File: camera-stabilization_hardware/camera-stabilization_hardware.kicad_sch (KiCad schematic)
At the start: 17 parts, among them J1 Conn_01x05_Pin, J2 Conn_01x05_Pin, J3 AVR-ISP-6, U1 ULN2003, U2 ULN2003, U3 ATmega328PB-A, Y1 Crystal_GND24

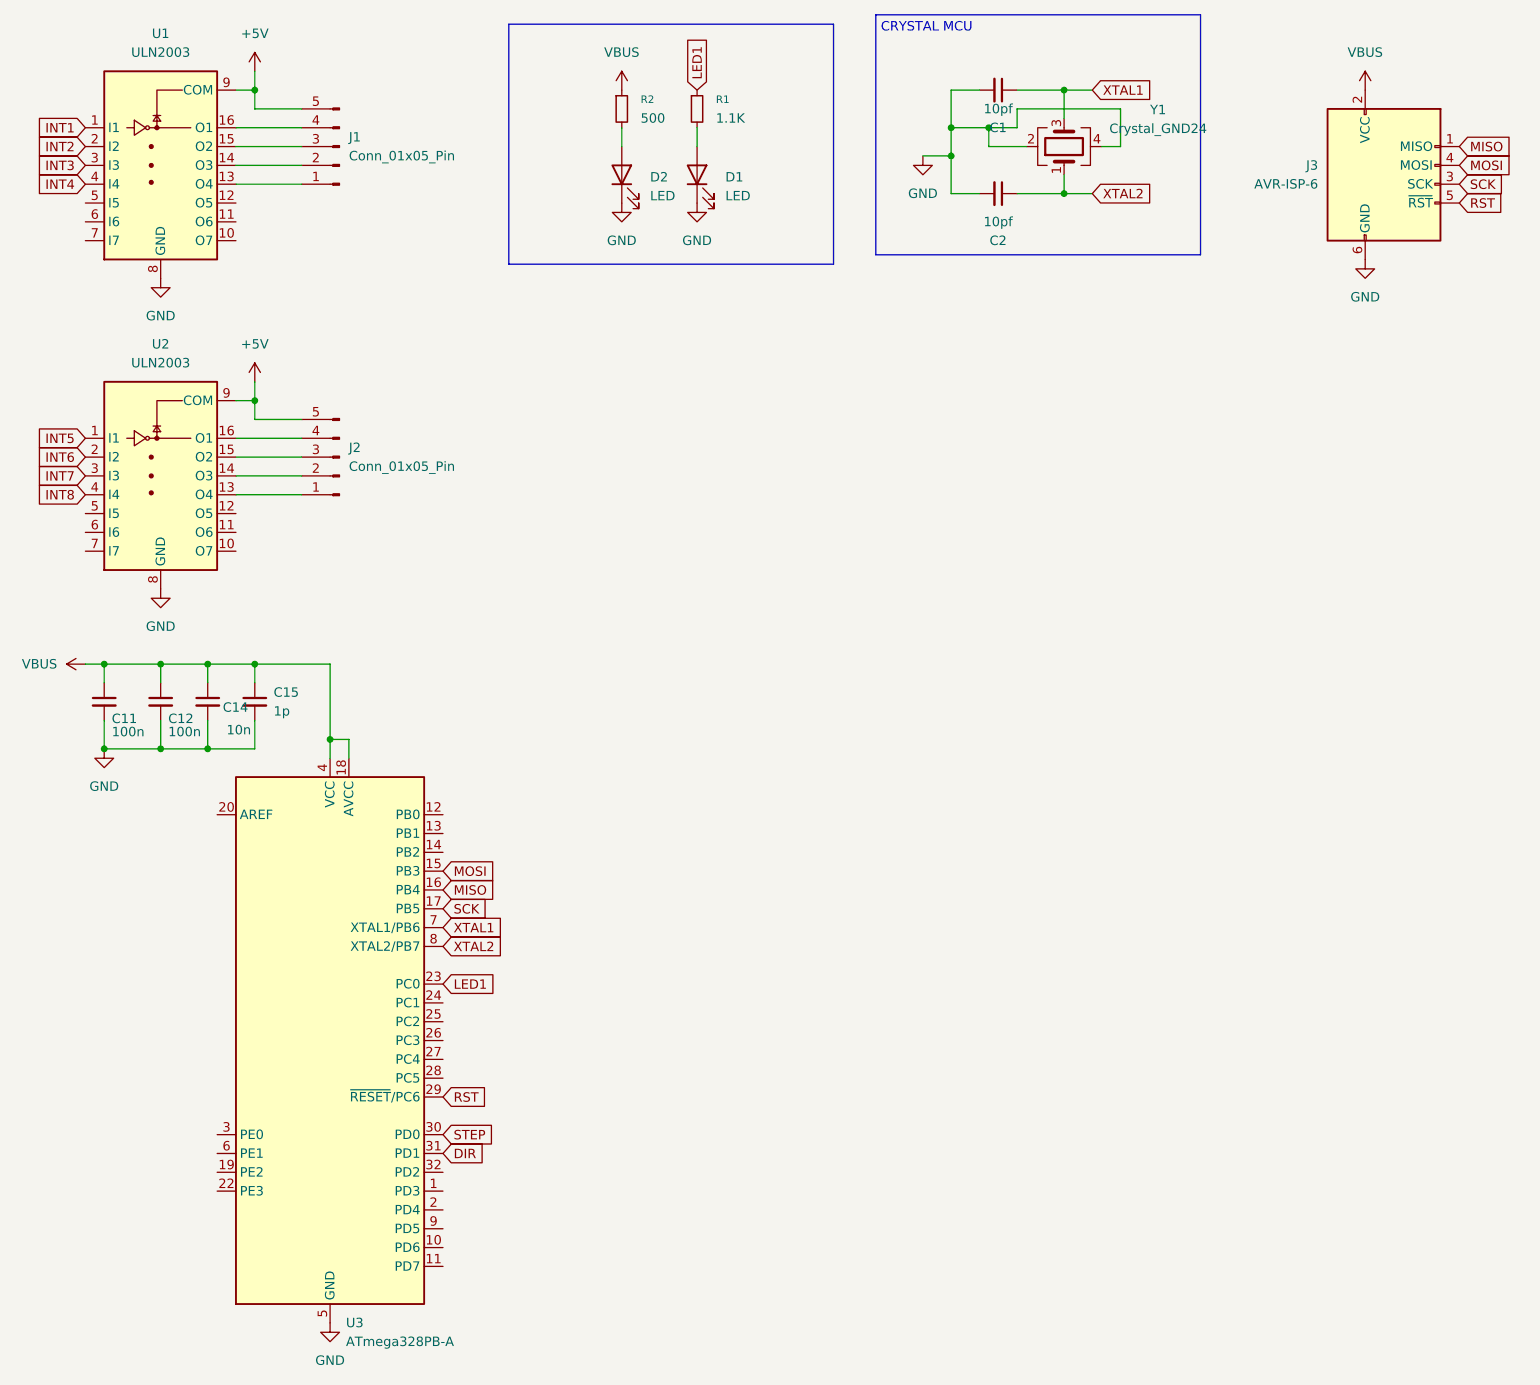
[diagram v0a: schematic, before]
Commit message: added pcb wiring camera stabilization
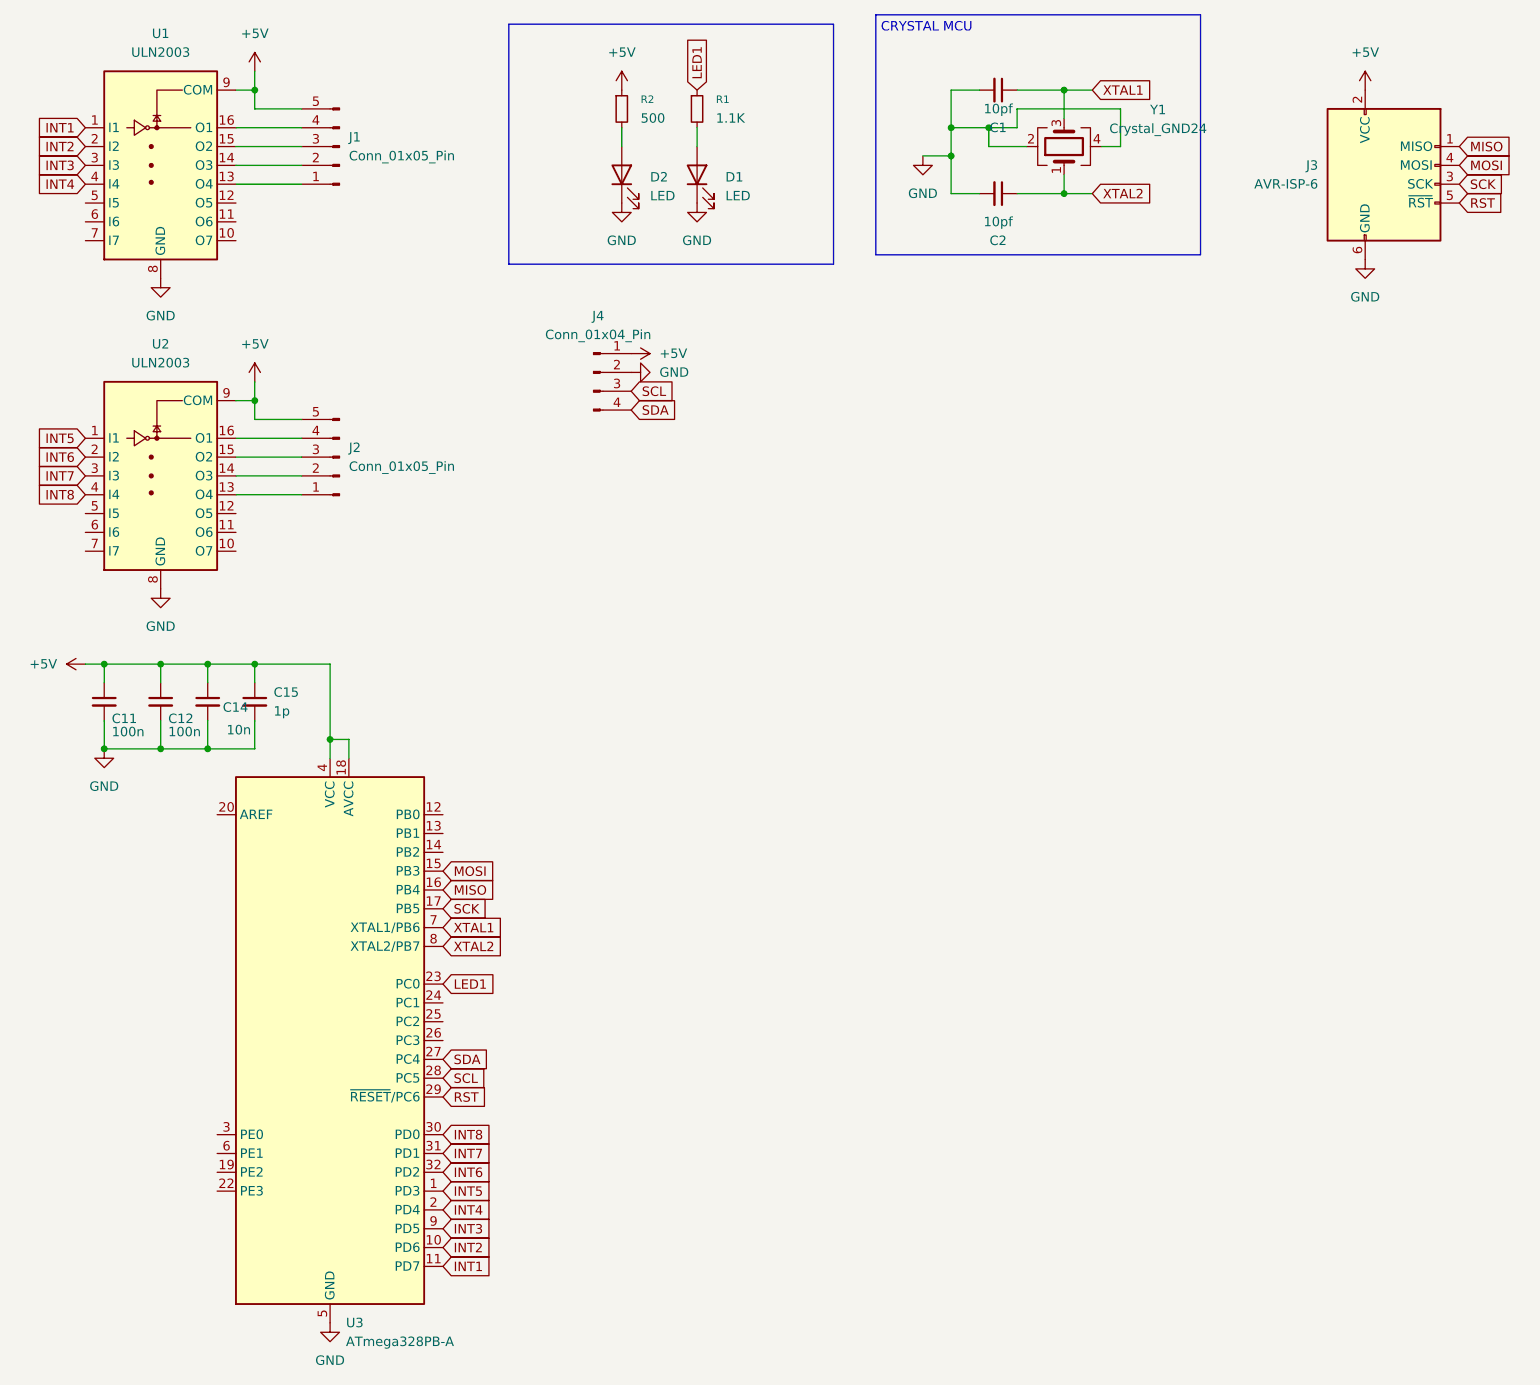
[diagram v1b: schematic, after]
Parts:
- added J4: Conn_01x04_Pin, Connector_JST:JST_SH_BM04B-SRSS-TB_1x04-1MP_P1.00mm_Vertical, symbol Connector:Conn_01x04_Pin
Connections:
- net DIR is gone; now on net INT7: U3.31 (PD1)
- net STEP is gone; now on net INT8: U3.30 (PD0)
- net VBUS is gone; now on net +5V: C11.1, C12.1, C14.1, C15.1, J3.2 (VCC), R2.1, U3.18 (AVCC), U3.4 (VCC)
- net +5V: now also J4.1 (Pin_1)
- net GND: now also J4.2 (Pin_2)
- net INT1: now also U3.11 (PD7)
- net INT2: now also U3.10 (PD6)
- net INT3: now also U3.9 (PD5)
- net INT4: now also U3.2 (PD4)
- net INT5: now also U3.1 (PD3)
- net INT6: now also U3.32 (PD2)
- net SDA: now reaches U3.27 (PC4)
- net SDA: now also J4.4 (Pin_4)
- net SCL: now reaches U3.28 (PC5)
- net SCL: now also J4.3 (Pin_3)

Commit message: add firmware
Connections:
- net +5V: now also U3.20 (AREF)
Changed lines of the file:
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@@
+	(wire
+		(pts
+			(xy 41.91 115.57) (xy 55.88 115.57)
+		)
+		(stroke
+			(width 0)
+			(type default)
+		)
+	)
 	(wire
 		(pts
@@
 	(wire
 		(pts
+			(xy 58.42 111.76) (xy 60.96 111.76)
+		)
+		(stroke
+			(width 0)
+			(type default)
+		)
+	)
+	(wire
+		(pts
 			(xy 142.24 24.13) (xy 146.05 24.13)
 		)
@@
 	(wire
 		(pts
+			(xy 41.91 121.92) (xy 41.91 115.57)
+		)
+		(stroke
+			(width 0)
+			(type default)
+		)
+	)
+	(wire
+		(pts
+			(xy 55.88 111.76) (xy 58.42 111.76)
+		)
+		(stroke
+			(width 0)
+			(type default)
+		)
+	)
+	(wire
+		(pts
 			(xy 60.96 111.76) (xy 60.96 114.3)
 		)
@@
 	(wire
 		(pts
+			(xy 55.88 115.57) (xy 55.88 111.76)
+		)
+		(stroke
+			(width 0)
+			(type default)
+		)
+	)
+	(wire
+		(pts
 			(xy 58.42 111.76) (xy 58.42 101.6)
 		)
@@
 	(wire
 		(pts
-			(xy 58.42 111.76) (xy 60.96 111.76)
-		)
-		(stroke
-			(width 0)
-			(type default)
-		)
-	)
-	(wire
-		(pts
 			(xy 58.42 114.3) (xy 58.42 111.76)
 		)
@@
 		)
 		(stroke
+			(width 0)
+			(type default)
+		)
+	)
+	(wire
+		(pts
+			(xy 43.18 121.92) (xy 41.91 121.92)
+		)
+		(stroke
